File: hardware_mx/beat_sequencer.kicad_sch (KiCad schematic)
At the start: 6 parts, among them SW1 SW_SPST, SW74 RotaryEncoder_Switch_MP

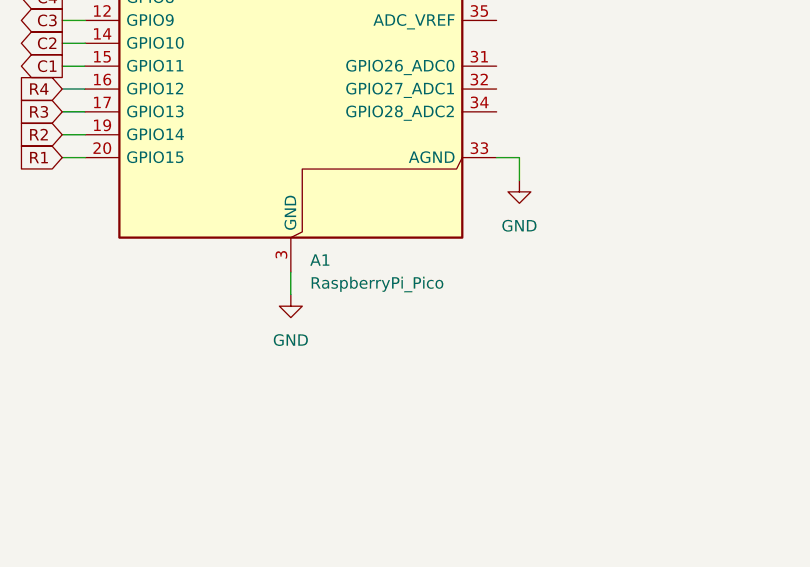
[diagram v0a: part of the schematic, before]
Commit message: Add mosfets to columns
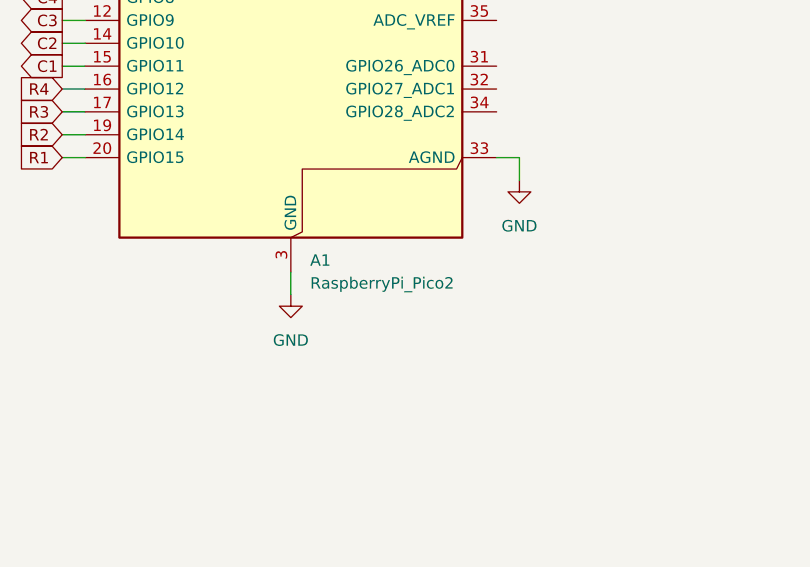
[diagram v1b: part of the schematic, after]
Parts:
- A1: value RaspberryPi_Pico -> RaspberryPi_Pico2
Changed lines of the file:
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@@
 			)
 		)
-		(property "Value" "RaspberryPi_Pico"
+		(property "Value" "RaspberryPi_Pico2"
 			(at 65.6433 116.84 0)
 			(effects
